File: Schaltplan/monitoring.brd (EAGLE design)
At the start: 100 x 80 mm, 19 parts, among them IC1 MEGA32-P

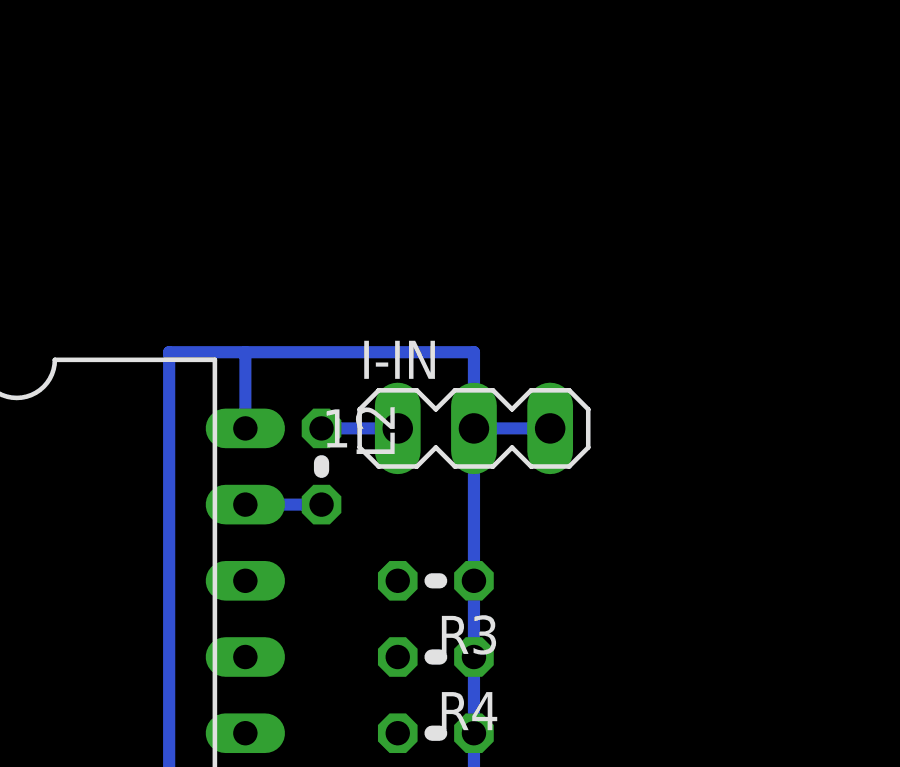
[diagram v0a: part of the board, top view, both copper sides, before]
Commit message: Use a median filter and an irr filter for the adc value which measures the current
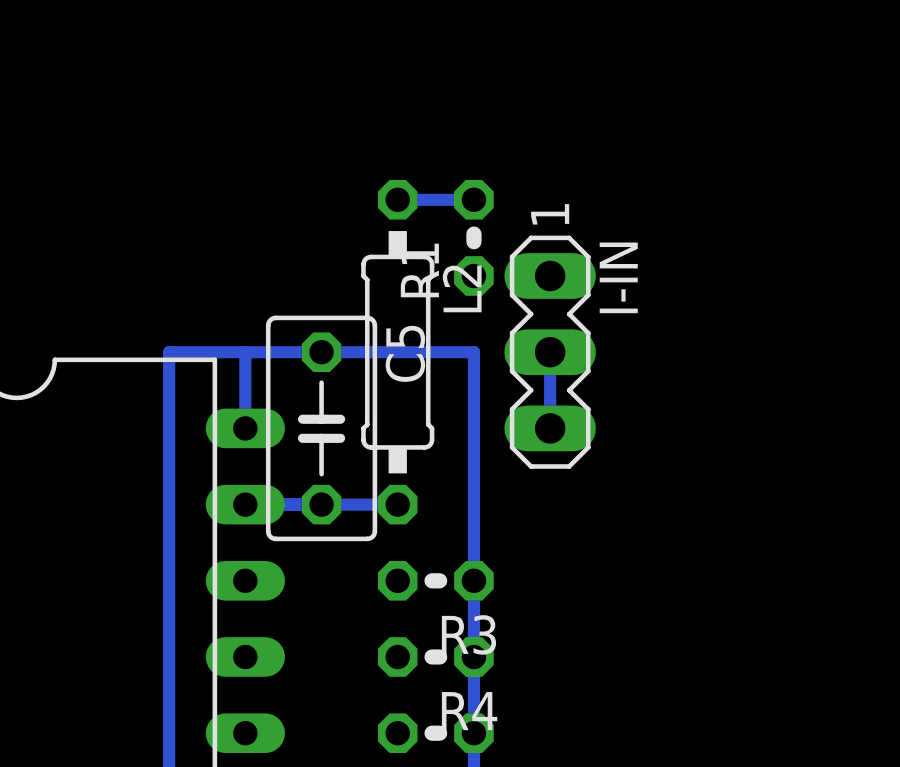
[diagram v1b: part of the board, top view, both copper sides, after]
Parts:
- added C5: 100n, rcl:C050-035X075
- added R1: 50k, rcl:0204V
- L2: device rcl:0204V -> rcl:0207/10
- moved L2 4.58 mm to (33.0, 61.0)
- moved I-IN 3.59 mm to (38.1, 61.0), turned to 270 degrees
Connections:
- removed net N$7: I-IN.1, L2.1
- new net N$21: L2.1, R1.2
- new net N$22: I-IN.1, R1.1
- net GND: now also C5.1
- net N$5: now also C5.2
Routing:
- net N$5: track 2.54 -> 7.62 mm
- net N$7: track 2.54 -> 0.00 mm
- net N$21: track 0.00 -> 2.54 mm
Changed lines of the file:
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@@
 <element name="D1" library="diode" package="DO41-10" value="1N4004" x="38.1" y="15.24" rot="R270"/>
 <element name="C1" library="rcl" package="E5-10,5" value="100µF" x="38.1" y="25.4" rot="R90"/>
-<element name="I-IN" library="con-lstb" package="MA03-1" value="" x="35.56" y="58.42">
-<attribute name="OC_NEWARK" value="unknown" x="74.93" y="17.78" size="1.778" layer="27" display="off"/>
-<attribute name="MPN" value="" x="74.93" y="17.78" size="1.778" layer="27" display="off"/>
-<attribute name="MF" value="" x="74.93" y="17.78" size="1.778" layer="27" display="off"/>
-<attribute name="OC_FARNELL" value="unknown" x="74.93" y="17.78" size="1.778" layer="27" display="off"/>
+<element name="I-IN" library="con-lstb" package="MA03-1" value="" x="38.1" y="60.96" rot="R270">
+<attribute name="OC_NEWARK" value="unknown" x="-2.54" y="21.59" size="1.778" layer="27" rot="R270" display="off"/>
+<attribute name="MPN" value="" x="-2.54" y="21.59" size="1.778" layer="27" rot="R270" display="off"/>
+<attribute name="MF" value="" x="-2.54" y="21.59" size="1.778" layer="27" rot="R270" display="off"/>
+<attribute name="OC_FARNELL" value="unknown" x="-2.54" y="21.59" size="1.778" layer="27" rot="R270" display="off"/>
 </element>
 <element name="LCD-DATA" library="con-lstb" package="MA04-1" value="" x="10.16" y="54.61" rot="R90">
@@
 <element name="C4" library="rcl" package="C050-035X075" value="100n" x="30.48" y="33.02" rot="R90"/>
 <element name="L1" library="rcl" package="0204V" value="10µ" x="35.56" y="31.75" rot="R270"/>
-<element name="L2" library="rcl" package="0204V" value="10µ" x="30.48" y="57.15" rot="R270"/>
+<element name="L2" library="rcl" package="0207/10" value="10µ" x="33.02" y="60.96" rot="R270"/>
+<element name="R1" library="rcl" package="0204V" value="50k" x="35.56" y="64.77" rot="R90"/>
+<element name="C5" library="rcl" package="C050-035X075" value="100n" x="30.48" y="58.42" rot="R270"/>
 </elements>
 <signals>
@@
 <wire x1="25.4" y1="60.96" x2="27.94" y2="60.96" width="0.4064" layer="16"/>
 <wire x1="27.94" y1="58.42" x2="27.94" y2="60.96" width="0.4064" layer="16"/>
-<wire x1="27.94" y1="60.96" x2="35.56" y2="60.96" width="0.4064" layer="16"/>
-<wire x1="35.56" y1="60.96" x2="35.56" y2="58.42" width="0.4064" layer="16"/>
 <wire x1="35.56" y1="40.64" x2="35.56" y2="43.18" width="0.4064" layer="16"/>
-<wire x1="35.56" y1="53.34" x2="35.56" y2="58.42" width="0.4064" layer="16"/>
 <wire x1="35.56" y1="50.8" x2="35.56" y2="53.34" width="0.4064" layer="16"/>
 <wire x1="35.56" y1="48.26" x2="35.56" y2="50.8" width="0.4064" layer="16"/>
 <wire x1="35.56" y1="45.72" x2="35.56" y2="43.18" width="0.4064" layer="16"/>
 <wire x1="35.56" y1="48.26" x2="35.56" y2="45.72" width="0.4064" layer="16"/>
-<wire x1="35.56" y1="58.42" x2="38.1" y2="58.42" width="0.4064" layer="16"/>
+<wire x1="38.1" y1="60.96" x2="38.1" y2="58.42" width="0.4064" layer="16"/>
 <wire x1="38.1" y1="27.94" x2="38.1" y2="35.56" width="0.4064" layer="16"/>
 <wire x1="38.1" y1="35.56" x2="35.56" y2="35.56" width="0.4064" layer="16"/>
+<contactref element="C5" pad="1"/>
+<wire x1="27.94" y1="60.96" x2="30.48" y2="60.96" width="0.4064" layer="16"/>
+<wire x1="35.56" y1="53.34" x2="35.56" y2="60.96" width="0.4064" layer="16"/>
+<wire x1="35.56" y1="60.96" x2="30.48" y2="60.96" width="0.4064" layer="16"/>
+<wire x1="35.56" y1="60.96" x2="38.1" y2="60.96" width="0" layer="19" extent="16-16"/>
+<wire x1="43.18" y1="17.78" x2="38.1" y2="27.94" width="0" layer="19" extent="1-1"/>
 <wire x1="43.18" y1="15.24" x2="43.18" y2="17.78" width="0" layer="19" extent="1-1"/>
-<wire x1="38.1" y1="27.94" x2="43.18" y2="17.78" width="0" layer="19" extent="1-1"/>
 </signal>
 <signal name="N$5">
 <contactref element="IC1" pad="39"/>
 <contactref element="L2" pad="2"/>
+<contactref element="C5" pad="2"/>
 <wire x1="27.94" y1="55.88" x2="30.48" y2="55.88" width="0.4064" layer="16"/>
-</signal>
-<signal name="N$7">
-<contactref element="I-IN" pad="1"/>
-<contactref element="L2" pad="1"/>
-<wire x1="30.48" y1="58.42" x2="33.02" y2="58.42" width="0.4064" layer="16"/>
+<wire x1="27.94" y1="55.88" x2="33.02" y2="55.88" width="0.4064" layer="16"/>
 </signal>
 <signal name="N$12">
@@
 <wire x1="35.56" y1="33.02" x2="30.48" y2="33.02" width="0.4064" layer="16"/>
 </signal>
+<signal name="N$21">
+<contactref element="R1" pad="2"/>
+<contactref element="L2" pad="1"/>
+<wire x1="33.02" y1="66.04" x2="35.56" y2="66.04" width="0.4064" layer="16"/>
+</signal>
+<signal name="N$22">
+<contactref element="R1" pad="1"/>
+<contactref element="I-IN" pad="1"/>
+<wire x1="35.56" y1="63.5" x2="38.1" y2="63.5" width="0" layer="19" extent="1-1"/>
+</signal>
 </signals>
